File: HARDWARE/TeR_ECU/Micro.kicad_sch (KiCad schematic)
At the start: 1 part, among them U1 NUCLEO-F446RE

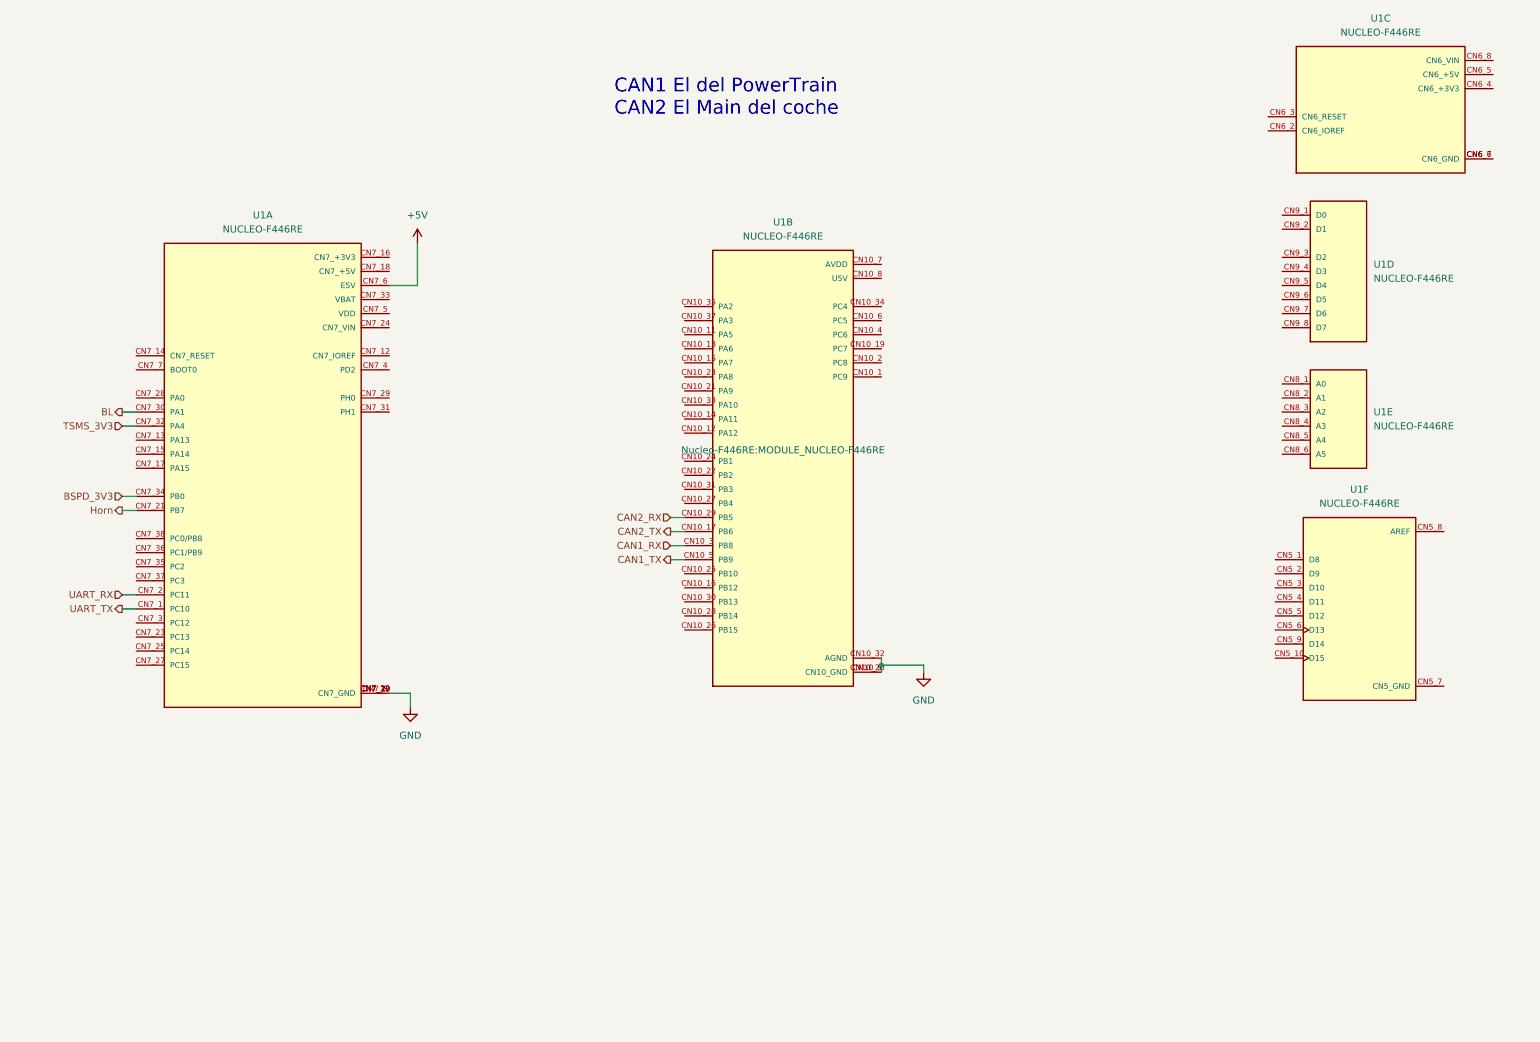
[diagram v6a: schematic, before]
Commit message: Finished re layout and adaption between the two versions
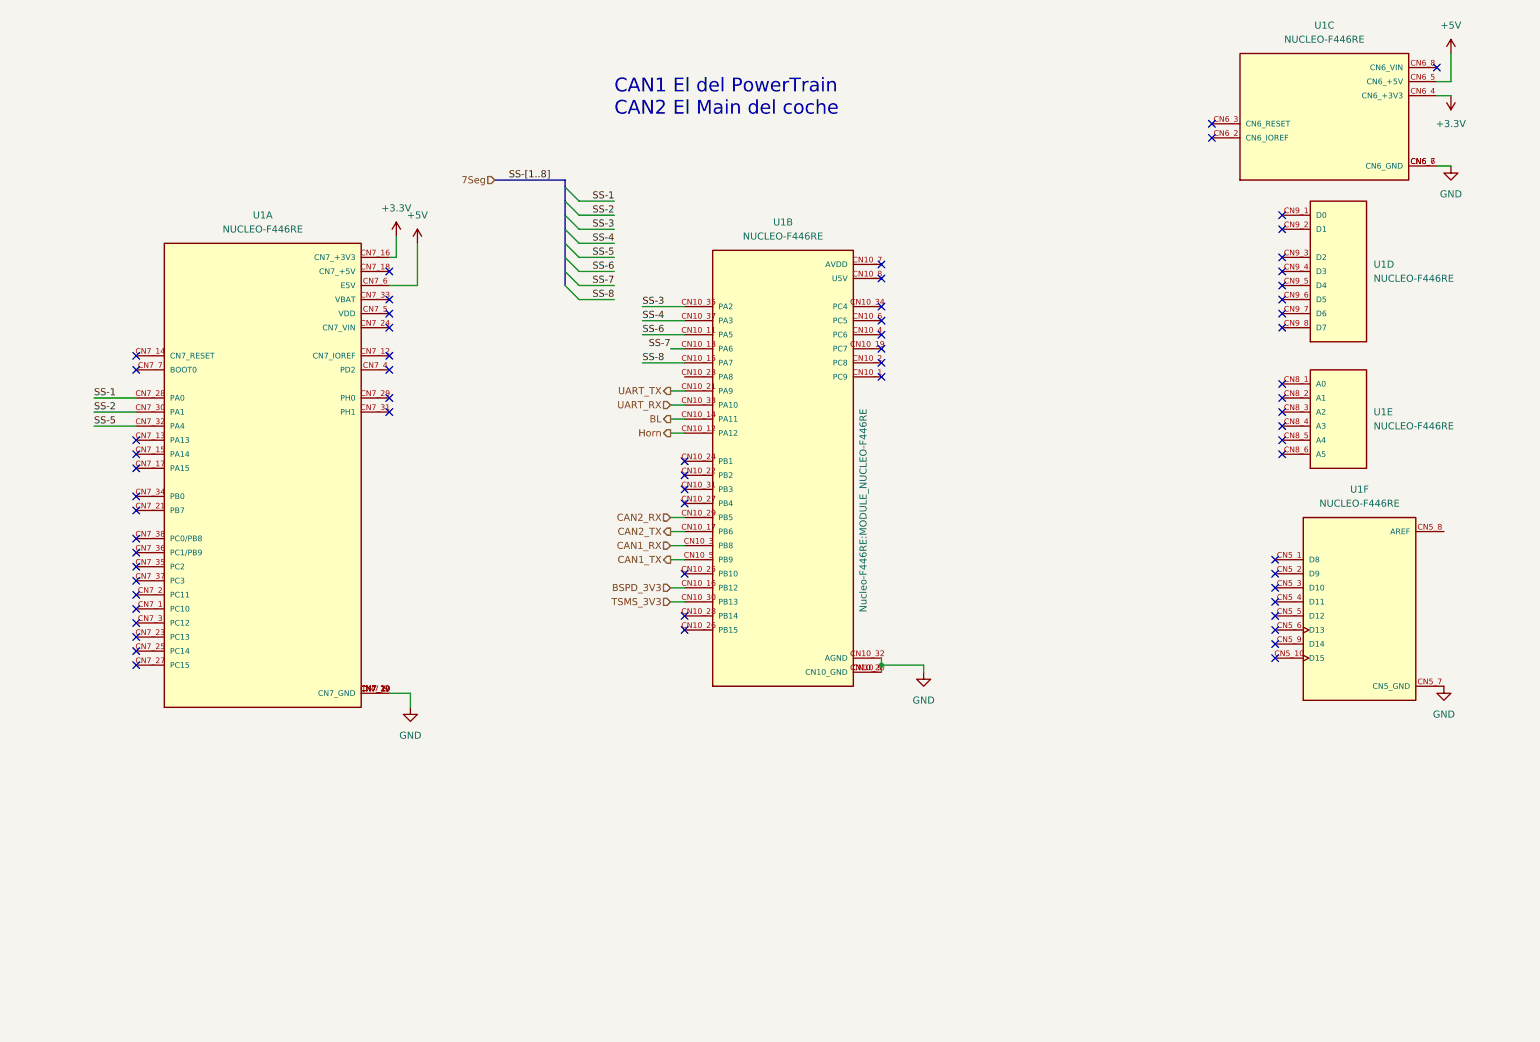
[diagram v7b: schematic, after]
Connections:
- net +5V: now also U1.CN6_5 (CN6_+5V)
- net BL: now also U1.CN10_14 (PA11); no longer U1.CN7_30 (PA1)
- net BSPD_3V3: now also U1.CN10_16 (PB12); no longer U1.CN7_34 (PB0)
- net GND: now also U1.CN5_7 (CN5_GND), U1.CN6_6 (CN6_GND), U1.CN6_7 (CN6_GND)
- net Horn: now also U1.CN10_12 (PA12); no longer U1.CN7_21 (PB7)
- net TSMS_3V3: now also U1.CN10_30 (PB13); no longer U1.CN7_32 (PA4)
- net UART_RX: now also U1.CN10_33 (PA10); no longer U1.CN7_2 (PC11)
- net UART_TX: now also U1.CN10_21 (PA9); no longer U1.CN7_1 (PC10)
- net +3.3V: now reaches U1.CN7_16 (CN7_+3V3)
- net +3.3V: now also U1.CN6_4 (CN6_+3V3)
- net SS-1: now reaches U1.CN7_28 (PA0)
- net SS-6: now reaches U1.CN10_11 (PA5)
- net SS-7: now reaches U1.CN10_13 (PA6)
- net SS-8: now reaches U1.CN10_15 (PA7)
- net SS-3: now reaches U1.CN10_35 (PA2)
- net SS-4: now reaches U1.CN10_37 (PA3)
- new net SS-2: U1.CN7_30 (PA1)
- new net SS-5: U1.CN7_32 (PA4)
- no-connect marks 0 -> 65
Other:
- moved on the sheet: U1C

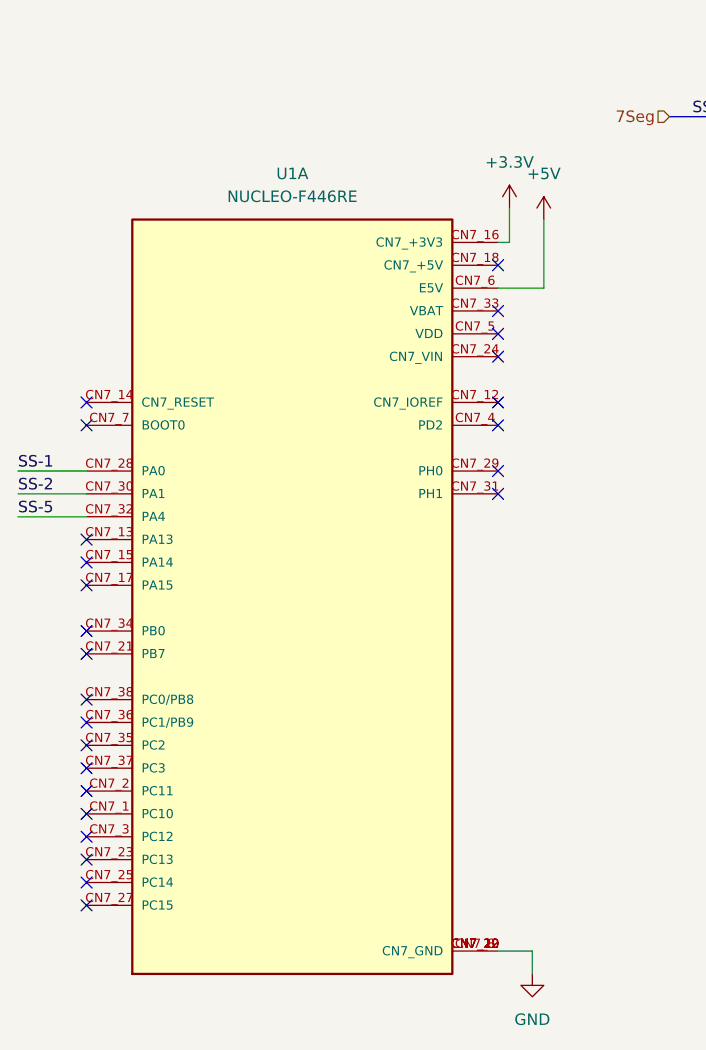
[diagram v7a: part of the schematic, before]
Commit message: Microcontroller f405 sketch started
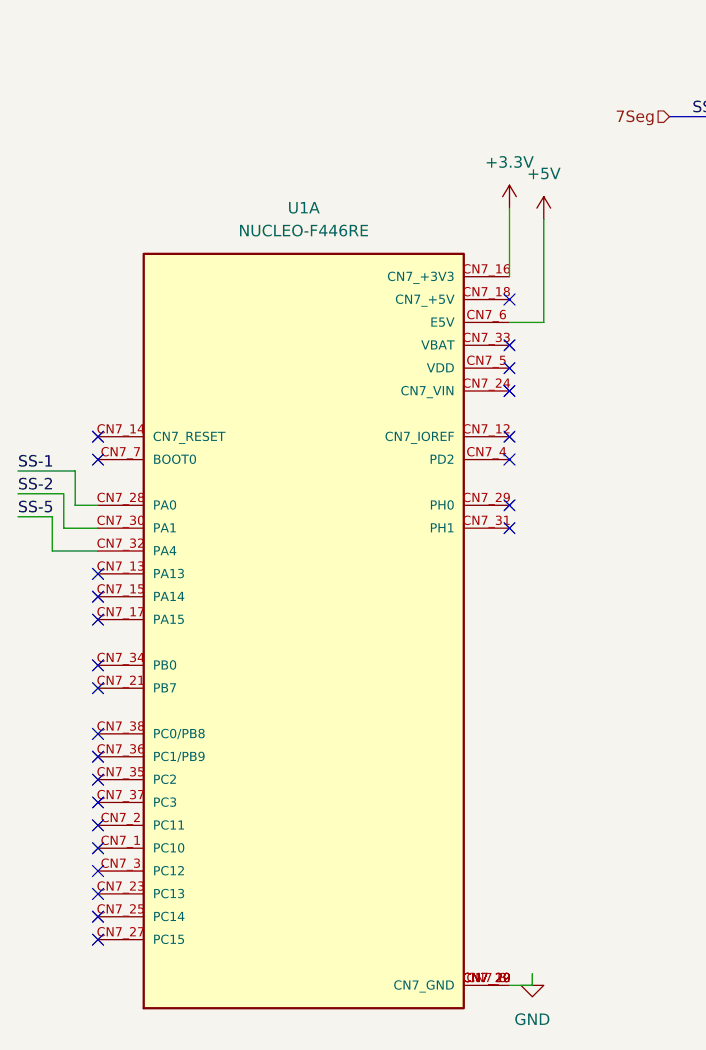
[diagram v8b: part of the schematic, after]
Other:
- moved on the sheet: U1A
